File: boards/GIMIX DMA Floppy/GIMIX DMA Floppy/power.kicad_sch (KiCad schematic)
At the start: 53 parts, among them Q1 LM7805_TO220, Q2 LM7805_TO220, U10 74LS393, U11 7404, U12 74LS74, U14 74LS08, U2 7438, U20 4538, U22 74LS123, U23 7406, U24 74LS74, U25 74LS74, U3 7438, U36 74F04, U37 7420, U38 74LS367, U39 74LS32, U4 7406, U40 74LS136, U41 74LS136, U42 74LS136, U43 74LS136, U44 74LS136, U45 74LS244, U46 74LS244, U5 7406, U52 74LS132, U55 7406, U59 74LS74, U6 74LS08, U7 74LS08, U9 74LS221

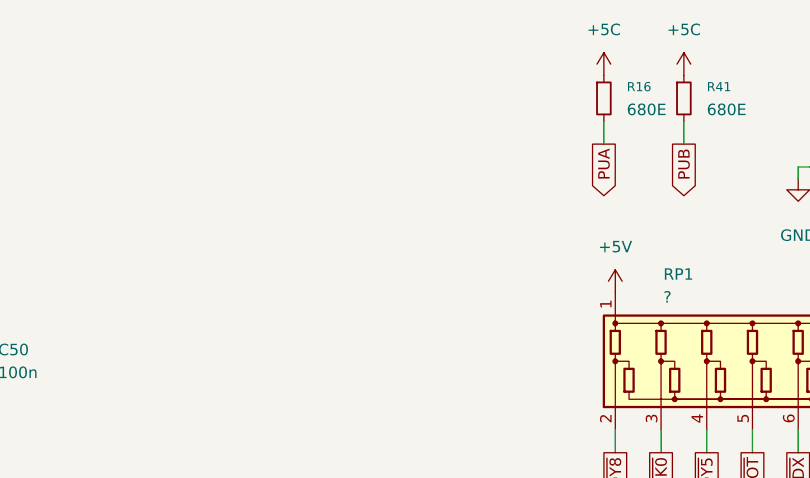
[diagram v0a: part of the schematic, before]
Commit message: DMA Floppy update, silkscreen and gerbers added
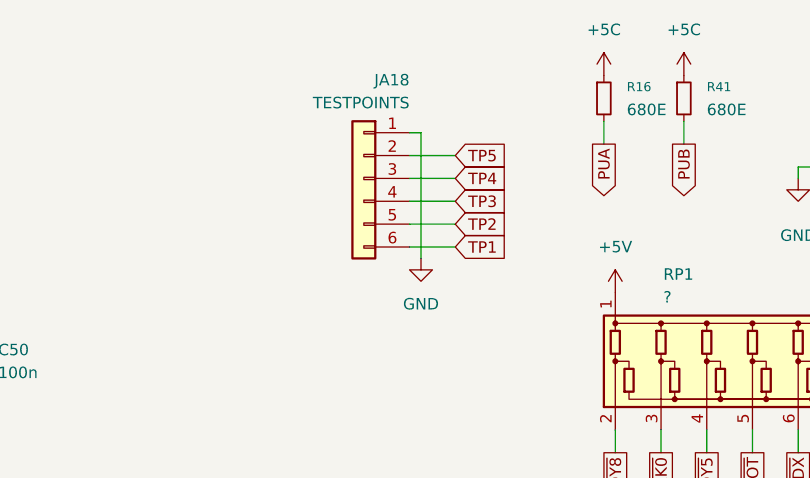
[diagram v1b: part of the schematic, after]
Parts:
- added JA18: TESTPOINTS, Connector_PinHeader_2.54mm:PinHeader_1x06_P2.54mm_Vertical, symbol Connector_Generic:Conn_01x06
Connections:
- net GND: now also JA18.1 (Pin_1)
- new net TP1: JA18.6 (Pin_6)
- new net TP2: JA18.5 (Pin_5)
- new net TP3: JA18.4 (Pin_4)
- new net TP4: JA18.3 (Pin_3)
- new net TP5: JA18.2 (Pin_2)
